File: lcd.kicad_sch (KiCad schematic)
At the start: 11 parts, among them J1 FPC-05F-12PH20, Q2 SS8050

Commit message: remove backups, removed old chip
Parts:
- removed C9: 10nF, Capacitor_SMD:C_0603_1608Metric, symbol Device:C
- removed J1: FPC-05F-12PH20, Connector_FFC-FPC:TE_1-1734839-2_1x12-1MP_P0.5mm_Horizontal, symbol Connector_Generic:Conn_01x12
- removed Q2: SS8050, Package_TO_SOT_SMD:SOT-23, symbol Transistor_BJT:SS8050
- removed R11, R12, R13, R14, R15: 10k, Resistor_SMD:R_0603_1608Metric, symbol Device:R
- removed R16: 180k, Resistor_SMD:R_0603_1608Metric, symbol Device:R
- removed R17: 20R, Resistor_SMD:R_0603_1608Metric, symbol Device:R
- removed R18: 1K, Resistor_SMD:R_0603_1608Metric, symbol Device:R
- added C27: 10nF, Capacitor_SMD:C_0603_1608Metric, symbol Device:C
- added J5: FPC-05F-12PH20, Connector_FFC-FPC:TE_4-1734839-0_1x40-1MP_P0.5mm_Horizontal, symbol Connector_Generic:Conn_01x40
- added Q3: SS8050, Package_TO_SOT_SMD:SOT-23, symbol Transistor_BJT:SS8050
- added R27: 30R, Resistor_SMD:R_0603_1608Metric, symbol Device:R
- added R28: 180k, Resistor_SMD:R_0603_1608Metric, symbol Device:R
- added R29: 1K, Resistor_SMD:R_0603_1608Metric, symbol Device:R
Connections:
- net +3V3: now also C27.2, J5.33 (Pin_33), J5.38 (Pin_38), J5.39 (Pin_39), J5.6 (Pin_6), J5.7 (Pin_7)
- net GND: now also C27.1, J5.16 (Pin_16), J5.37 (Pin_37), J5.40 (Pin_40), J5.5 (Pin_5), Q3.2 (E), R28.2
- net LCD_BL: now also R29.2
- net LCD_CS: now also J5.9 (Pin_9)
- net LCD_RS: now also J5.12 (Pin_12)
- net LCD_RST: now also J5.15 (Pin_15)
- net LCD_SCL: now also J5.10 (Pin_10)
- net LCD_SDA: now also J5.13 (Pin_13)
- new net: Q3.1 (B), R28.1, R29.1
- new net: Q3.3 (C), R27.2
- new net: J5.34 (Pin_34), J5.35 (Pin_35), J5.36 (Pin_36), R27.1
- new net LCD_DC: J5.11 (Pin_11)
- new net LCD_FMARK: J5.8 (Pin_8)
- no-connect marks 1 -> 21
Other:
- note added: "4-wire 8-bit spi"
- note added: "https://nl.aliexpress.com/item/1005008112942872.html"
- note added: "parallel bus"
- note added: "shield example: https://www.buydisplay.com/3-2-inch-240x320-ips-tft-lcd-module-for-arduino-and-raspberry-pi"
- note added: "touch panel"
- note removed: "HS20HS072RX display"

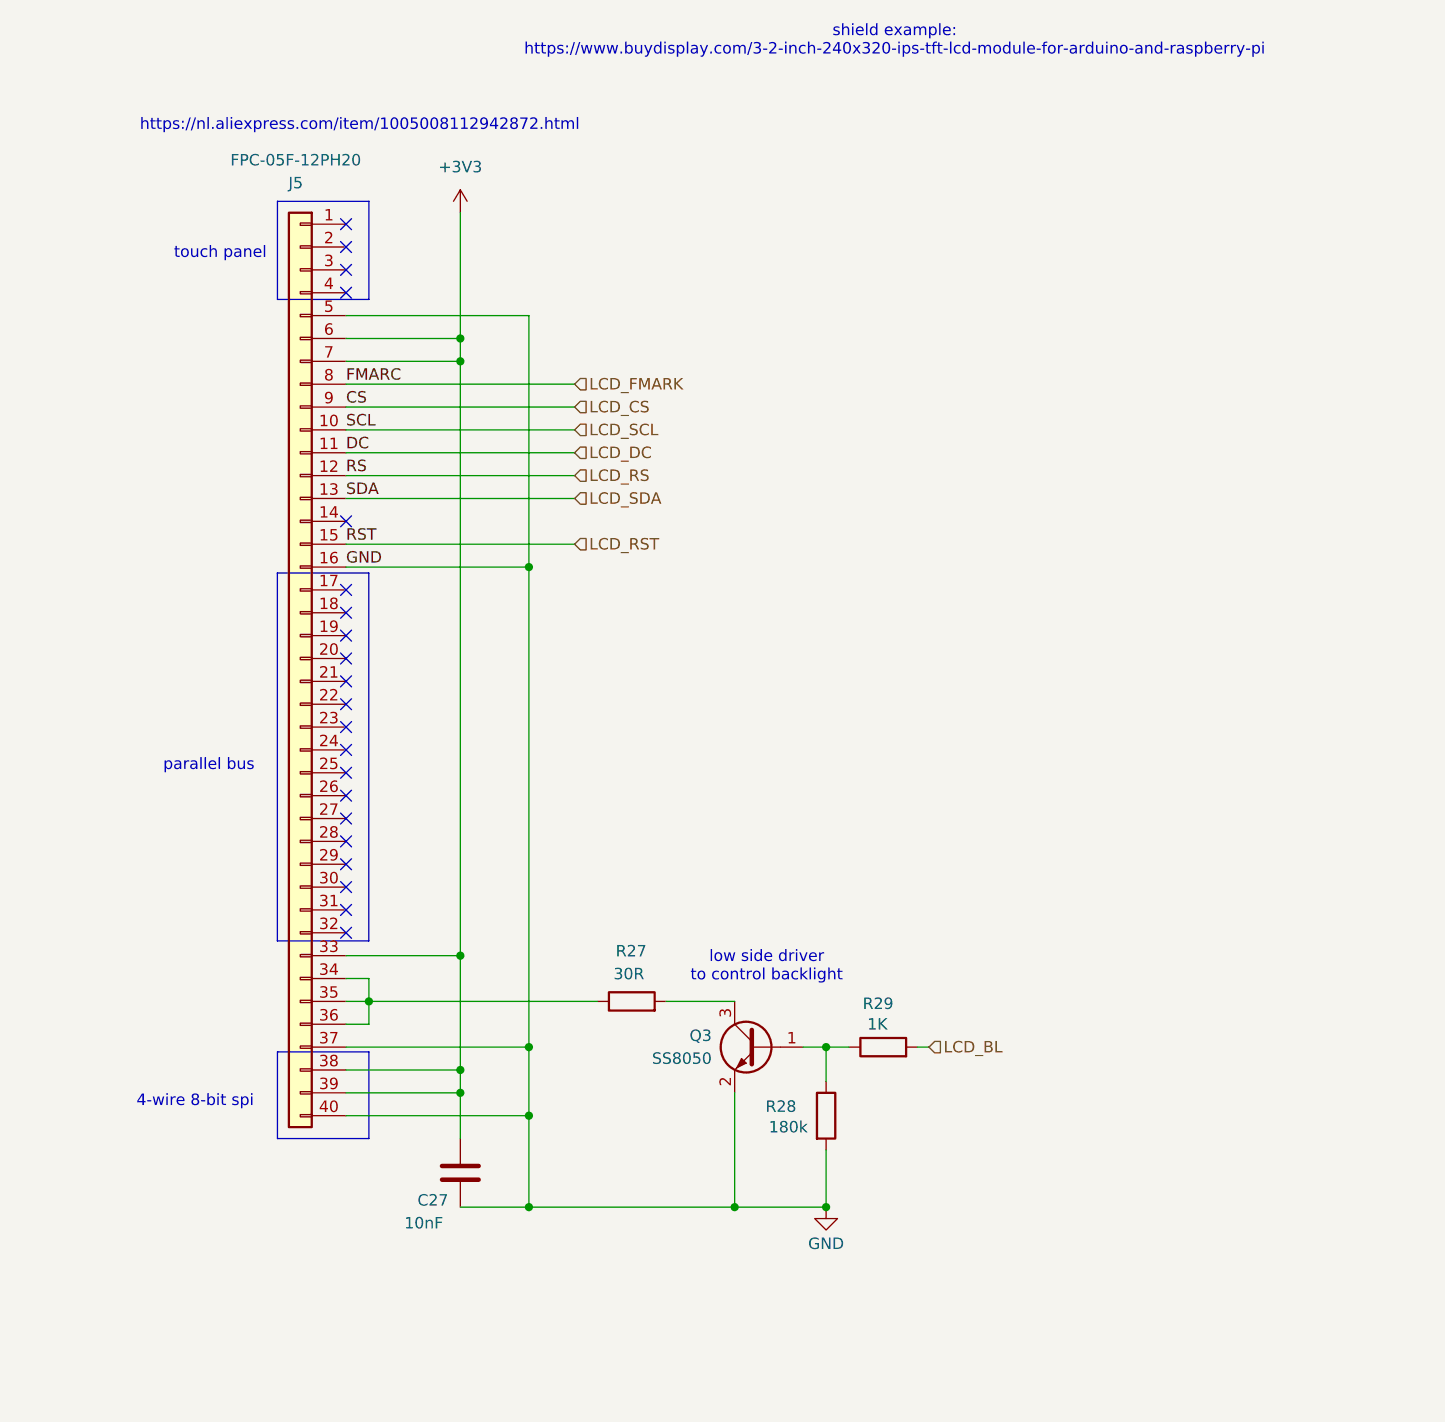
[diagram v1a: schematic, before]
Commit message: schematic functional and includes current test setup
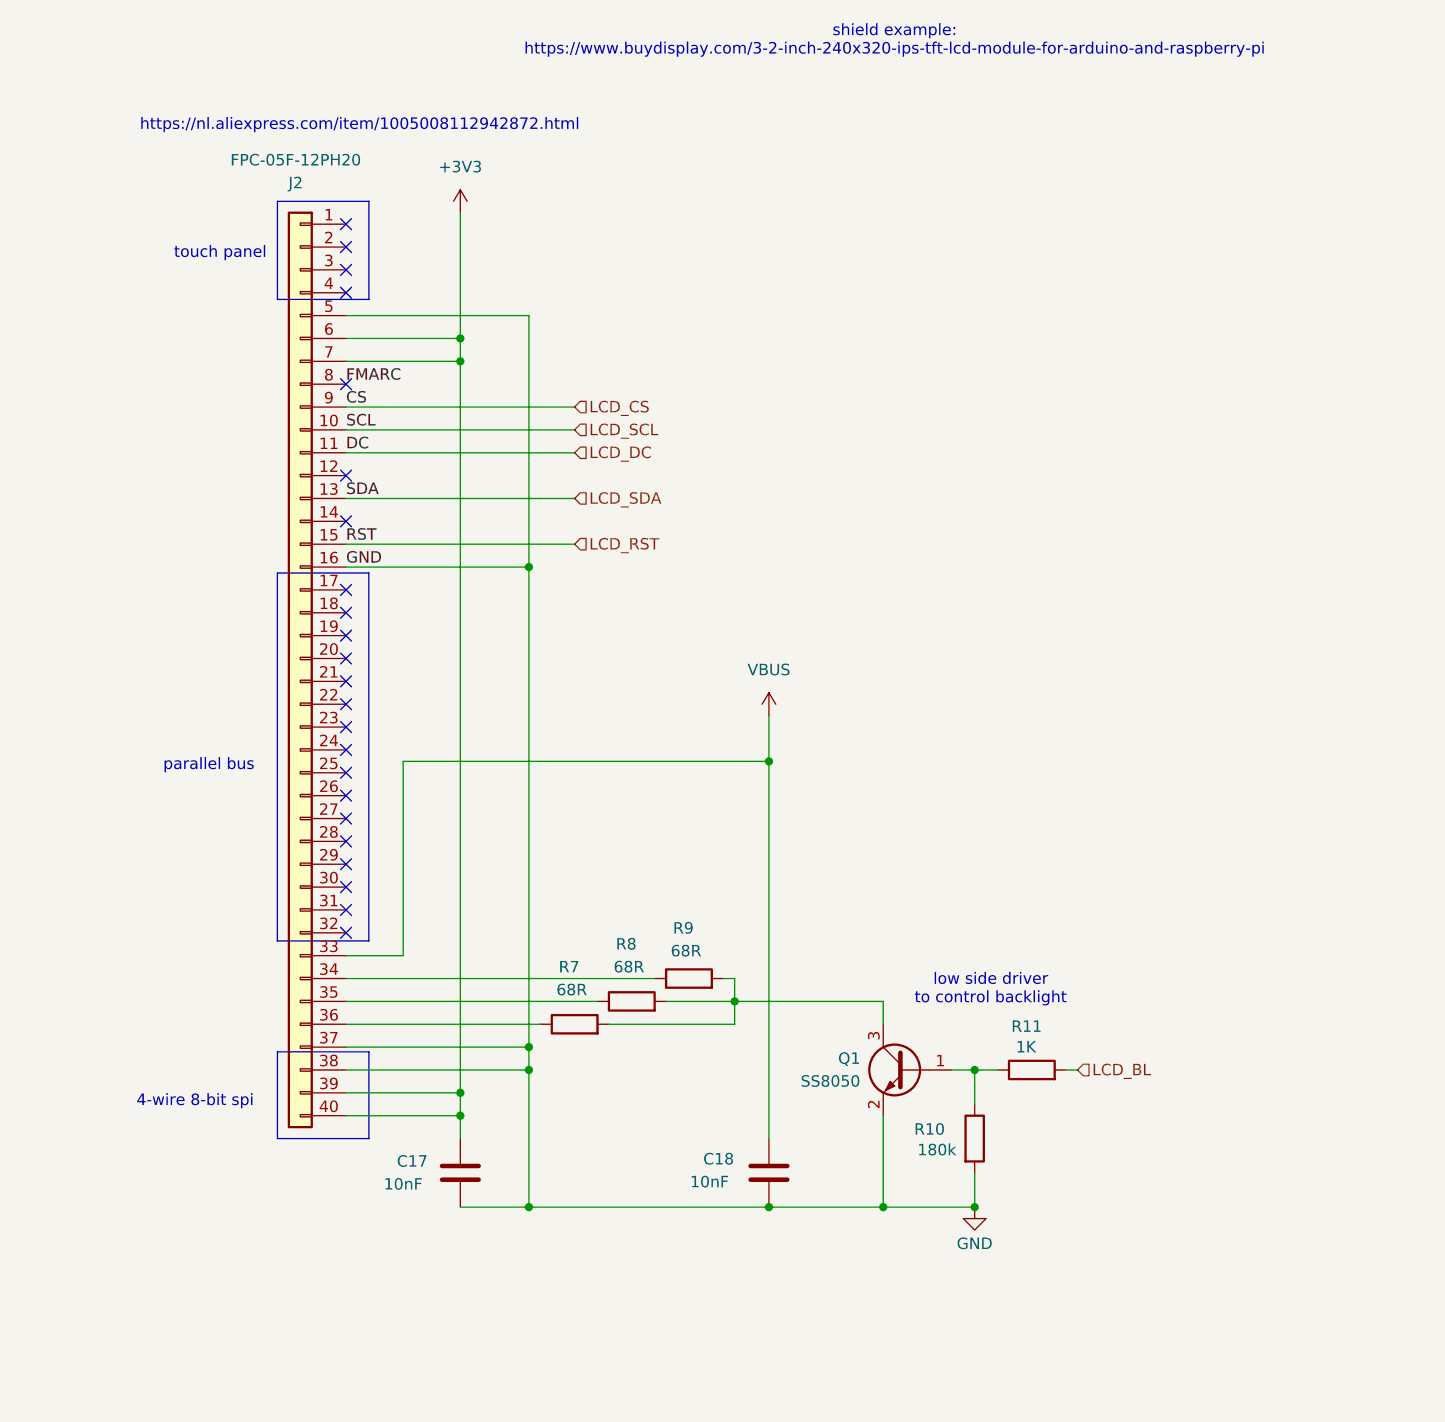
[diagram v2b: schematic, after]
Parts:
- added C18: 10nF, Capacitor_SMD:C_0603_1608Metric, symbol Device:C
- added R7, R9: 68R, Resistor_SMD:R_0603_1608Metric, symbol Device:R
- R8: renamed from R27; value 30R -> 68R
- renumbered C27 to C17, J5 to J2, Q3 to Q1, R28 to R10, R29 to R11
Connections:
- net +3V3: now also J2.40 (Pin_40); no longer J2.33 (Pin_33), J2.38 (Pin_38)
- net GND: now also J2.38 (Pin_38), C18.1; no longer J2.40 (Pin_40)
- net at Q1.3 (C), R8.2: now also R7.2, R9.2
- net at J2.35 (Pin_35), R8.1: no longer J2.34 (Pin_34), J2.36 (Pin_36)
- net LCD_FMARK renamed FMARC
- net LCD_RS: no longer names the net of J2.12 (Pin_12)
- new net: J2.36 (Pin_36), R7.1
- new net: J2.34 (Pin_34), R9.1
- new net VBUS: C18.2, J2.33 (Pin_33)
- no-connect marks 21 -> 23
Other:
- moved on the sheet: Q1, R10, R11

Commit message: add audio amp
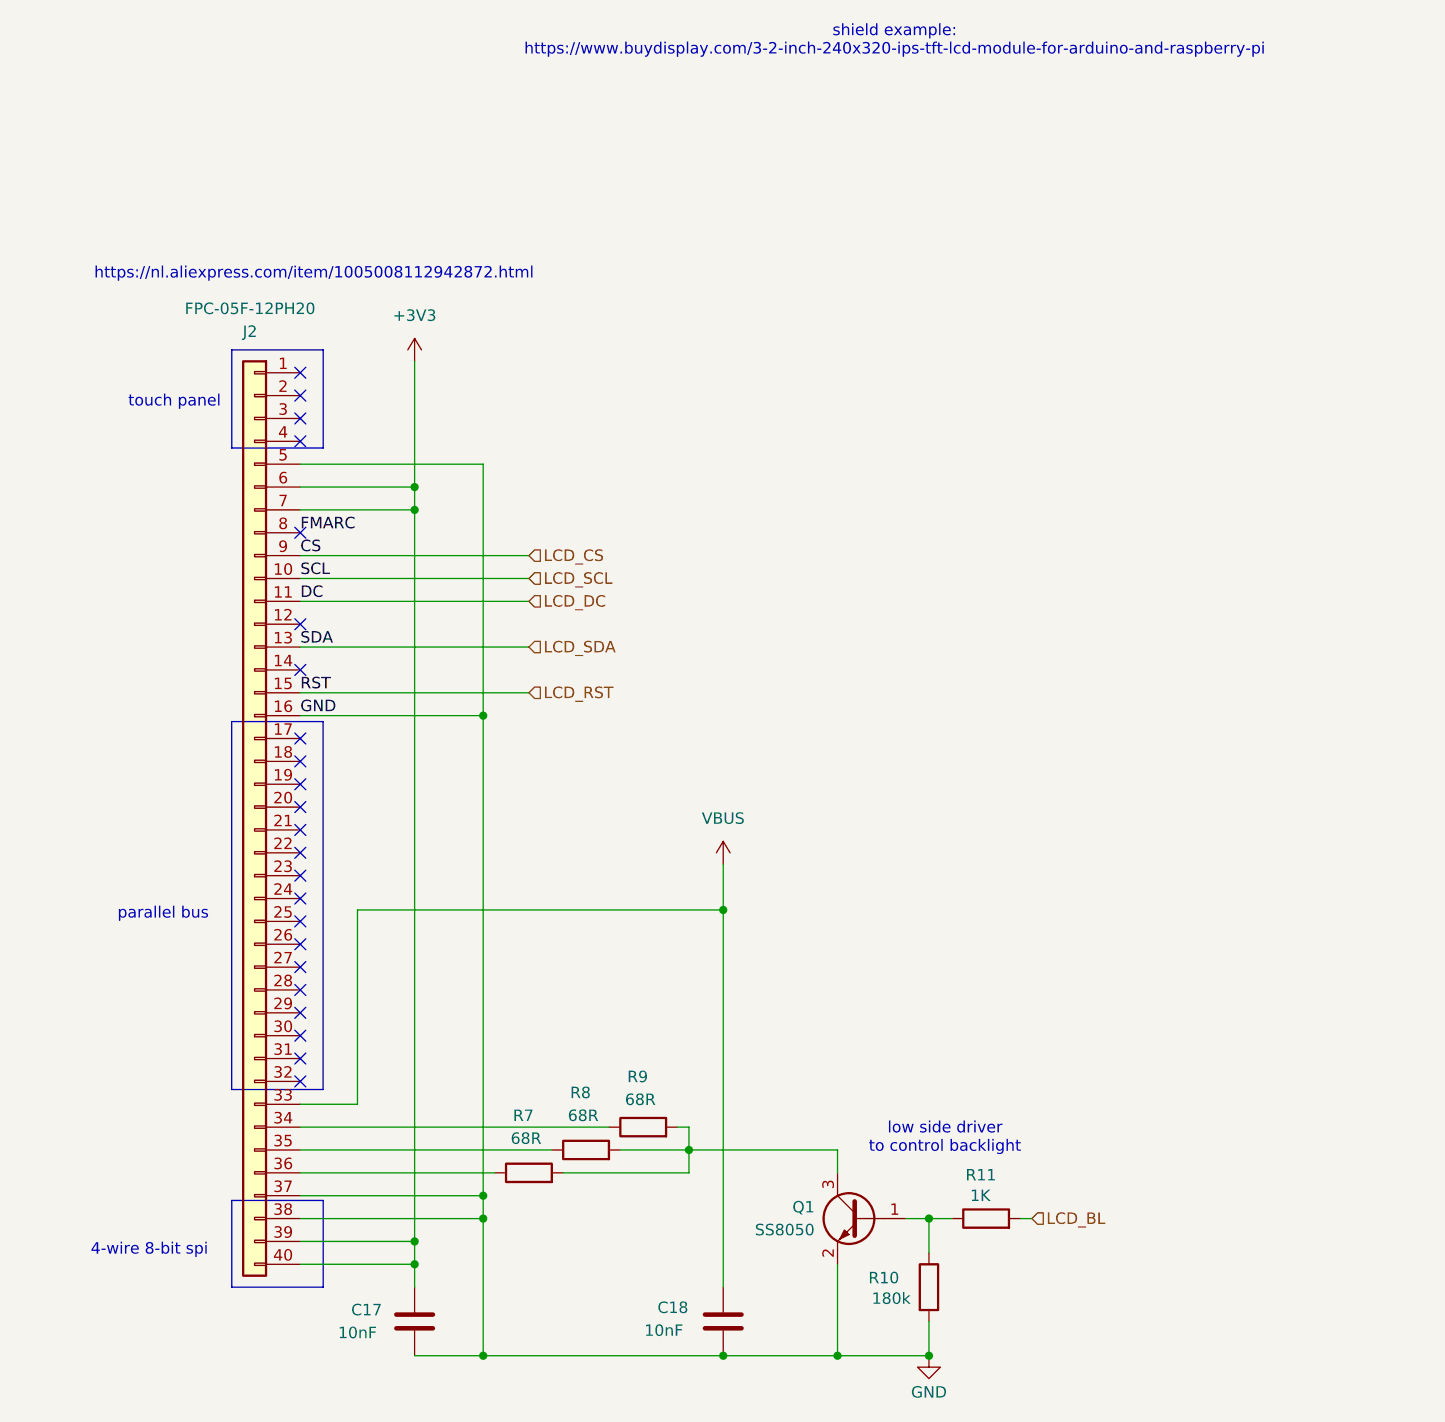
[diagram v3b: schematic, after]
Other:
- moved on the sheet: C17, C18, J2, Q1, R10, R11, R7, R8, R9

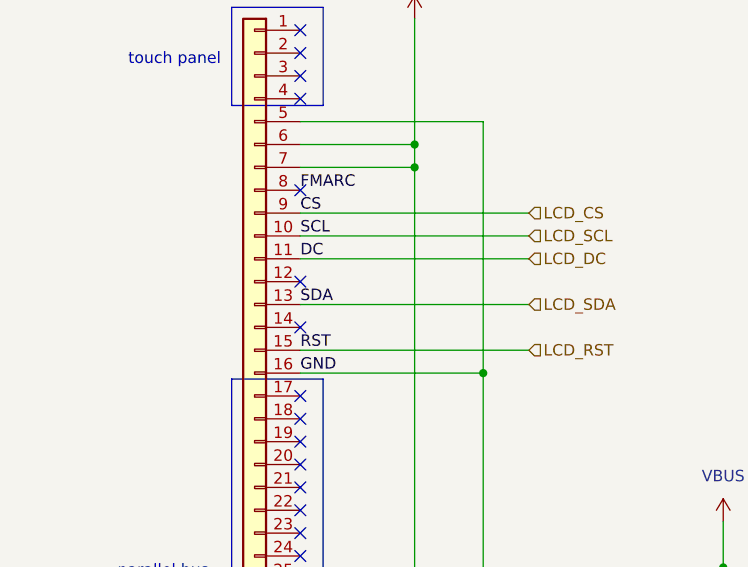
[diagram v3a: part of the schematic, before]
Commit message: add amplifier mode selector, add drawing lcd
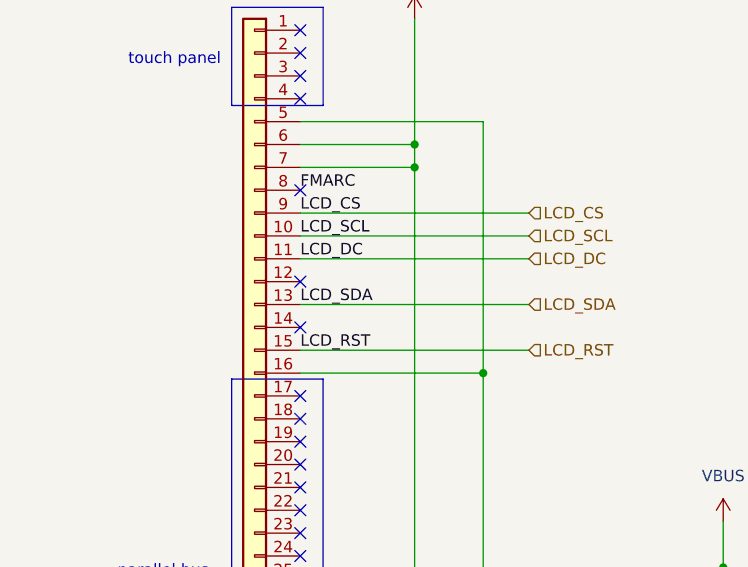
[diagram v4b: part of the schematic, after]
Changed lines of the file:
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@@
 		)
 	)
-	(label "RST"
+	(label "LCD_RST"
 		(at 74.93 95.25 0)
 		(effects
@@
 		)
 	)
-	(label "SDA"
+	(label "LCD_SDA"
 		(at 74.93 90.17 0)
 		(effects
@@
 		)
 	)
-	(label "GND"
-		(at 74.93 97.79 0)
-		(effects
-			(font
-				(size 1.27 1.27)
-			)
-			(justify left bottom)
-		)
-	)
-	(label "DC"
+	(label "LCD_DC"
 		(at 74.93 85.09 0)
 		(effects
@@
 		)
 	)
-	(label "SCL"
+	(label "LCD_SCL"
 		(at 74.93 82.55 0)
 		(effects
@@
 		)
 	)
-	(label "CS"
+	(label "LCD_CS"
 		(at 74.93 80.01 0)
 		(effects

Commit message: add on/off switch
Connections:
- net VBUS renamed +5V
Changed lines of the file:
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@@
+	)
+	(symbol
+		(lib_id "power:+5V")
+		(at 121.92 114.3 0)
+		(unit 1)
+		(exclude_from_sim no)
+		(in_bom yes)
+		(on_board yes)
+		(dnp no)
+		(fields_autoplaced yes)
+		(property "Reference" "#PWR033"
+			(at 121.92 118.11 0)
+			(effects
+				(font
+					(size 1.27 1.27)
+				)
+				(hide yes)
+			)
+		)
+		(property "Value" "+5V"
+			(at 121.92 109.22 0)
+			(effects
+				(font
+					(size 1.27 1.27)
+				)
+			)
+		)
+		(property "Footprint" ""
+			(at 121.92 114.3 0)
+			(effects
+				(font
+					(size 1.27 1.27)
+				)
+				(hide yes)
+			)
+		)
+		(property "Datasheet" ""
+			(at 121.92 114.3 0)
+			(effects
+				(font
+					(size 1.27 1.27)
+				)
+				(hide yes)
+			)
+		)
+		(property "Description" "Power symbol creates a global label with name \"+5V\""
+			(at 121.92 114.3 0)
+			(effects
+				(font
+					(size 1.27 1.27)
+				)
+				(hide yes)
+			)
+		)
+		(pin "1"
+		)
+		(instances
+			(project "gameboy"
+				(path "/f4643692-c319-40a7-82a2-3e775c0a417f/d0993c89-522c-4206-a2f2-b5b66c7e7b73"
+					(reference "#PWR033")
+					(unit 1)
+				)
+			)
+		)
 	)
 	(symbol
@@
 					(unit 1)
 				)
-			)
-		)
-	)
-	(symbol
-		(lib_id "power:VBUS")
-		(at 121.92 114.3 0)
-		(unit 1)
-		(exclude_from_sim no)
-		(in_bom yes)
-		(on_board yes)
-		(dnp no)
-		(fields_autoplaced yes)
-		(property "Reference" "#PWR019"
-			(at 121.92 118.11 0)
-			(effects
-				(font
-					(size 1.27 1.27)
-				)
-				(hide yes)
-			)
-		)
-		(property "Value" "VBUS"
-			(at 121.92 109.22 0)
-			(effects
-				(font
-					(size 1.27 1.27)
-				)
-			)
-		)
-		(property "Footprint" ""
-			(at 121.92 114.3 0)
-			(effects
-				(font
-					(size 1.27 1.27)
-				)
-				(hide yes)
-			)
-		)
-		(property "Datasheet" ""
-			(at 121.92 114.3 0)
-			(effects
-				(font
-					(size 1.27 1.27)
-				)
-				(hide yes)
-			)
-		)
-		(property "Description" "Power symbol creates a global label with name \"VBUS\""
-			(at 121.92 114.3 0)
-			(effects
-				(font
-					(size 1.27 1.27)
-				)
-				(hide yes)
-			)
-		)
-		(pin "1"
-		)
-		(instances
-			(project ""
-				(path "/f4643692-c319-40a7-82a2-3e775c0a417f/d0993c89-522c-4206-a2f2-b5b66c7e7b73"
-					(reference "#PWR019")
-					(unit 1)
-				)

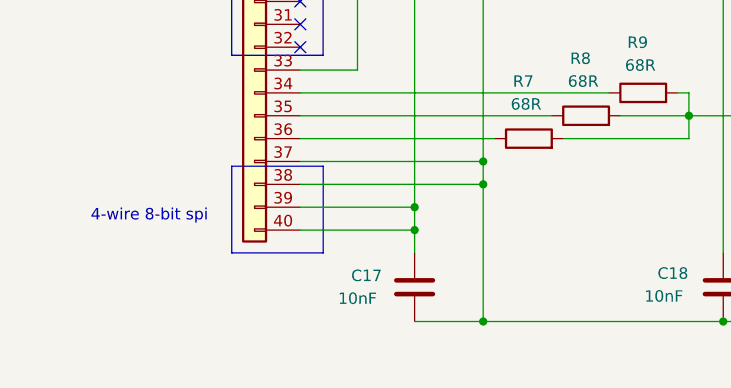
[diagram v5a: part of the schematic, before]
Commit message: add SD card
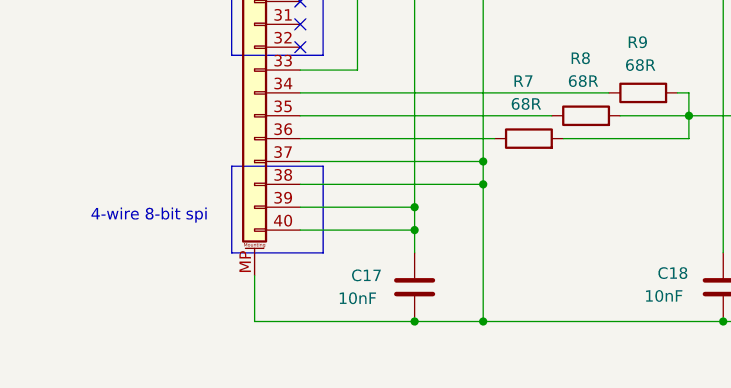
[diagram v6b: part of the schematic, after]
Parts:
- J2: symbol Connector_Generic:Conn_01x40 -> Connector_Generic_MountingPin:Conn_01x40_MountingPin
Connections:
- net GND: now also J2.MP (MountPin)
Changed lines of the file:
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@@
+	)
+	(junction
+		(at 87.63 168.91)
+		(diameter 0)
+		(color 0 0 0 0)
 	)
 	(junction
@@
 	(wire
 		(pts
+			(xy 69.85 168.91) (xy 87.63 168.91)
+		)
+		(stroke
+			(width 0)
+			(type default)
+		)
+	)
+	(wire
+		(pts
 			(xy 74.93 151.13) (xy 95.25 151.13)
 		)
@@
 		(pts
 			(xy 121.92 168.91) (xy 134.62 168.91)
+		)
+		(stroke
+			(width 0)
+			(type default)
+		)
+	)
+	(wire
+		(pts
+			(xy 69.85 163.83) (xy 69.85 168.91)
 		)
 		(stroke
@@
 	)
 	(symbol
-		(lib_id "Connector_Generic:Conn_01x40")
+		(lib_id "Connector_Generic_MountingPin:Conn_01x40_MountingPin")
 		(at 69.85 107.95 0)
 		(mirror y)
@@
 			)
 		)
-		(property "Description" "Generic connector, single row, 01x40, script generated (kicad-library-utils/schlib/autogen/connector/)"
+		(property "Description" "Generic connectable mounting pin connector, single row, 01x40, script generated (kicad-library-utils/schlib/autogen/connector/)"
 			(at 69.85 107.95 0)
 			(effects
@@
 		(pin "38"
 		)
+		(pin "MP"
+		)
 		(instances
